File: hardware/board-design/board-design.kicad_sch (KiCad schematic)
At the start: 0 parts

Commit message: feat(symbol): add a symbol for Gate-Driver
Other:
- added sheet DC-DC-Buck-Converter (DC-DC-Buck-Converter.kicad_sch)
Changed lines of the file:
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@@
 	(generator_version "10.0")
 	(paper "A4")
+	(sheet
+		(at 114.3 114.3)
+		(size 25.4 25.4)
+		(exclude_from_sim no)
+		(in_bom yes)
+		(on_board yes)
+		(dnp no)
+		(fields_autoplaced yes)
+		(stroke
+			(width 0.1524)
+			(type solid)
+		)
+		(fill
+			(color 0 0 0 0)
+		)
+		(property "Sheetname" "DC-DC-Buck-Converter"
+			(at 114.3 113.5884 0)
+			(show_name no)
+			(do_not_autoplace no)
+			(effects
+				(font
+					(size 1.27 1.27)
+				)
+				(justify left bottom)
+			)
+		)
+		(property "Sheetfile" "DC-DC-Buck-Converter.kicad_sch"
+			(at 114.3 140.2846 0)
+			(hide yes)
+			(show_name no)
+			(do_not_autoplace no)
+			(effects
+				(font
+					(size 1.27 1.27)
+				)
+				(justify left top)
+			)
+		)
+		(instances
+			(project "board-design"
+				(path "/bd5d7a3e-3306-4abd-ba38-3ca87df9a9fb"
+					(page "2")
+				)
+			)
+		)
+	)
 	(sheet_instances
 		(path "/"

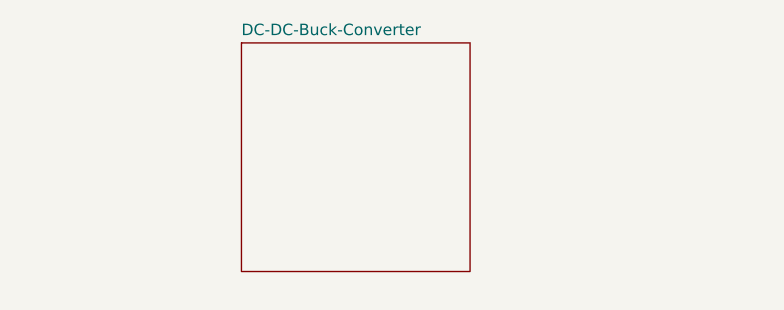
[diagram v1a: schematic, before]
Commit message: hw(schematic): complete Buck Converter schematic design
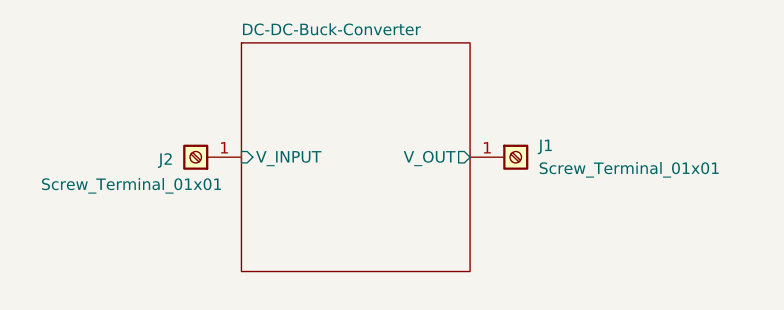
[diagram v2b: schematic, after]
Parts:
- added J1, J2: Screw_Terminal_01x01, symbol Connector:Screw_Terminal_01x01
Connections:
- new net DC-DC-Buck-Converter/V_INPUT: J2.1 (Pin_1)
- new net DC-DC-Buck-Converter/V_OUT: J1.1 (Pin_1)
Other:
- sheet DC-DC-Buck-Converter ports: added V_INPUT, V_OUT; removed none
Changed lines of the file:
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@@
 	(generator_version "10.0")
 	(paper "A4")
+	(symbol
+		(lib_id "Connector:Screw_Terminal_01x01")
+		(at 109.22 127 180)
+		(unit 1)
+		(body_style 1)
+		(exclude_from_sim no)
+		(in_bom yes)
+		(on_board yes)
+		(in_pos_files yes)
+		(dnp no)
+		(property "Reference" "J2"
+			(at 105.918 127.254 0)
+			(show_name no)
+			(do_not_autoplace no)
+			(effects
+				(font
+					(size 1.27 1.27)
+				)
+			)
+		)
+		(property "Value" "Screw_Terminal_01x01"
+			(at 102.108 130.048 0)
+			(show_name no)
+			(do_not_autoplace no)
+			(effects
+				(font
+					(size 1.27 1.27)
+				)
+			)
+		)
+		(property "Footprint" ""
+			(at 109.22 127 0)
+			(hide yes)
+			(show_name no)
+			(do_not_autoplace no)
+			(effects
+				(font
+					(size 1.27 1.27)
+				)
+			)
+		)
+		(property "Datasheet" ""
+			(at 109.22 127 0)
+			(hide yes)
+			(show_name no)
+			(do_not_autoplace no)
+			(effects
+				(font
+					(size 1.27 1.27)
+				)
+			)
+		)
+		(property "Description" "Generic screw terminal, single row, 01x01, script generated (kicad-library-utils/schlib/autogen/connector/)"
+			(at 109.22 127 0)
+			(hide yes)
+			(show_name no)
+			(do_not_autoplace no)
+			(effects
+				(font
+					(size 1.27 1.27)
+				)
+			)
+		)
+		(pin "1"
+		)
+		(instances
+			(project "board-design"
+				(path "/bd5d7a3e-3306-4abd-ba38-3ca87df9a9fb"
+					(reference "J2")
+					(unit 1)
+				)
+			)
+		)
+	)
+	(symbol
+		(lib_id "Connector:Screw_Terminal_01x01")
+		(at 144.78 127 0)
+		(unit 1)
+		(body_style 1)
+		(exclude_from_sim no)
+		(in_bom yes)
+		(on_board yes)
+		(in_pos_files yes)
+		(dnp no)
+		(fields_autoplaced yes)
+		(property "Reference" "J1"
+			(at 147.32 125.7299 0)
+			(show_name no)
+			(do_not_autoplace no)
+			(effects
+				(font
+					(size 1.27 1.27)
+				)
+				(justify left)
+			)
+		)
+		(property "Value" "Screw_Terminal_01x01"
+			(at 147.32 128.2699 0)
+			(show_name no)
+			(do_not_autoplace no)
+			(effects
+				(font
+					(size 1.27 1.27)
+				)
+				(justify left)
+			)
+		)
+		(property "Footprint" ""
+			(at 144.78 127 0)
+			(hide yes)
+			(show_name no)
+			(do_not_autoplace no)
+			(effects
+				(font
+					(size 1.27 1.27)
+				)
+			)
+		)
+		(property "Datasheet" ""
+			(at 144.78 127 0)
+			(hide yes)
+			(show_name no)
+			(do_not_autoplace no)
+			(effects
+				(font
+					(size 1.27 1.27)
+				)
+			)
+		)
+		(property "Description" "Generic screw terminal, single row, 01x01, script generated (kicad-library-utils/schlib/autogen/connector/)"
+			(at 144.78 127 0)
+			(hide yes)
+			(show_name no)
+			(do_not_autoplace no)
+			(effects
+				(font
+					(size 1.27 1.27)
+				)
+			)
+		)
+		(pin "1"
+		)
+		(instances
+			(project "board-design"
+				(path "/bd5d7a3e-3306-4abd-ba38-3ca87df9a9fb"
+					(reference "J1")
+					(unit 1)
+				)
+			)
+		)
+	)
 	(sheet
 		(at 114.3 114.3)
@@
 			)
 		)
+		(pin "V_INPUT" input
+			(at 114.3 127 180)
+			(effects
+				(font
+					(size 1.27 1.27)
+				)
+				(justify left)
+			)
+		)
+		(pin "V_OUT" output
+			(at 139.7 127 0)
+			(effects
+				(font
+					(size 1.27 1.27)
+				)
+				(justify right)
+			)
+		)

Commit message: hw(schematic): update schematic and finally complate ()
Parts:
- added J3: Screw_Terminal_01x01, symbol Connector:Screw_Terminal_01x01
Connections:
- new net DC-DC-Buck-Converter/VDD: J3.1 (Pin_1)
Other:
- sheet DC-DC-Buck-Converter ports: added VDD; removed none
- moved on the sheet: J2
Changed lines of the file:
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@@
 	(symbol
 		(lib_id "Connector:Screw_Terminal_01x01")
-		(at 109.22 127 180)
+		(at 109.22 119.38 180)
 		(unit 1)
 		(body_style 1)
@@
 		(dnp no)
 		(property "Reference" "J2"
-			(at 105.918 127.254 0)
+			(at 105.918 119.634 0)
 			(show_name no)
 			(do_not_autoplace no)
@@
 		)
 		(property "Value" "Screw_Terminal_01x01"
-			(at 102.108 130.048 0)
+			(at 102.108 122.428 0)
 			(show_name no)
 			(do_not_autoplace no)
@@
 		)
 		(property "Footprint" ""
-			(at 109.22 127 0)
+			(at 109.22 119.38 0)
 			(hide yes)
 			(show_name no)
@@
 		)
 		(property "Datasheet" ""
-			(at 109.22 127 0)
+			(at 109.22 119.38 0)
 			(hide yes)
 			(show_name no)
@@
 		)
 		(property "Description" "Generic screw terminal, single row, 01x01, script generated (kicad-library-utils/schlib/autogen/connector/)"
-			(at 109.22 127 0)
+			(at 109.22 119.38 0)
 			(hide yes)
 			(show_name no)
@@
 		)
 	)
+	(symbol
+		(lib_id "Connector:Screw_Terminal_01x01")
+		(at 109.22 133.35 180)
+		(unit 1)
+		(body_style 1)
+		(exclude_from_sim no)
+		(in_bom yes)
+		(on_board yes)
+		(in_pos_files yes)
+		(dnp no)
+		(property "Reference" "J3"
+			(at 105.918 133.604 0)
+			(show_name no)
+			(do_not_autoplace no)
+			(effects
+				(font
+					(size 1.27 1.27)
+				)
+			)
+		)
+		(property "Value" "Screw_Terminal_01x01"
+			(at 102.108 136.398 0)
+			(show_name no)
+			(do_not_autoplace no)
+			(effects
+				(font
+					(size 1.27 1.27)
+				)
+			)
+		)
+		(property "Footprint" ""
+			(at 109.22 133.35 0)
+			(hide yes)
+			(show_name no)
+			(do_not_autoplace no)
+			(effects
+				(font
+					(size 1.27 1.27)
+				)
+			)
+		)
+		(property "Datasheet" ""
+			(at 109.22 133.35 0)
+			(hide yes)
+			(show_name no)
+			(do_not_autoplace no)
+			(effects
+				(font
+					(size 1.27 1.27)
+				)
+			)
+		)
+		(property "Description" "Generic screw terminal, single row, 01x01, script generated (kicad-library-utils/schlib/autogen/connector/)"
+			(at 109.22 133.35 0)
+			(hide yes)
+			(show_name no)
+			(do_not_autoplace no)
+			(effects
+				(font
+					(size 1.27 1.27)
+				)
+			)
+		)
+		(pin "1"
+		)
+		(instances
+			(project "board-design"
+				(path "/bd5d7a3e-3306-4abd-ba38-3ca87df9a9fb"
+					(reference "J3")
+					(unit 1)
+				)
+			)
+		)
+	)
 	(sheet
 		(at 114.3 114.3)
@@
 		)
 		(pin "V_INPUT" input
-			(at 114.3 127 180)
+			(at 114.3 119.38 180)
 			(effects
 				(font
@@
 			)
 		)
+		(pin "VDD" input
+			(at 114.3 133.35 180)
+			(effects
+				(font
+					(size 1.27 1.27)
+				)
+				(justify left)
+			)
+		)

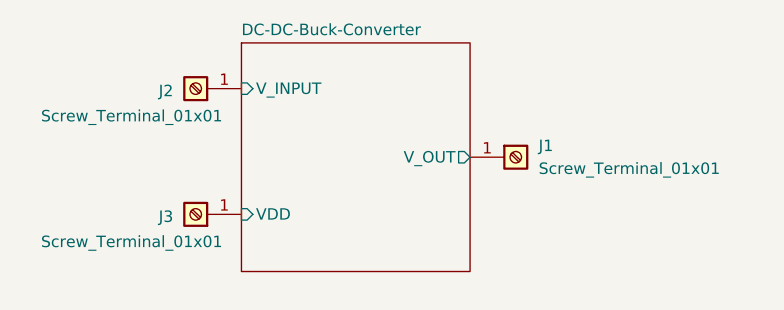
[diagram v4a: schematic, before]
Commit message: add new values and information to fields and
Updated and rearranged the schema.
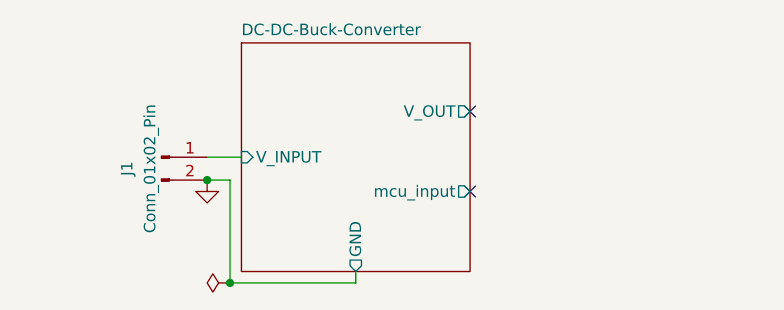
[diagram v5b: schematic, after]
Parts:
- removed J1, J2, J3: Screw_Terminal_01x01, symbol Connector:Screw_Terminal_01x01
- added J1: Conn_01x02_Pin, Connector_Molex:Molex_Micro-Fit_3.0_43650-0212_1x02-1MP_P3.00mm_Horizontal, symbol Connector:Conn_01x02_Pin
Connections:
- net DC-DC-Buck-Converter/V_INPUT: now also J1.1 (Pin_1)
- new net GND: J1.2 (Pin_2)
- no-connect marks 0 -> 2
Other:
- sheet DC-DC-Buck-Converter ports: added GND, mcu_input; removed VDD
